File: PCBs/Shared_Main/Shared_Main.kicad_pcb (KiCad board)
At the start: 4 copper layers, 185.4 x 55.9 mm, 53 parts, among them J1 Power, J10 Digital inputs, J11 Digital inputs, J12 Digital inputs, J13 Digital inputs, J14 Digital inputs, J15 Digital inputs, J16 Other unit, J2 Rotary switches pin 1, J4 Aux, J5 Analog inputs, J7 Keypad, Q1 BC547, Q2 BC547, Q3 BC547, Q4 BC547, Q5 BC547, Q6 BC547, Q7 BC547, Q8 BC547, U1 ESP32-S3-ZERO, U2 74HC4051, U4 74HC165, U5 74HC165, U6 74HC165, U7 74HC165, U8 74HC165, U9 74HC165

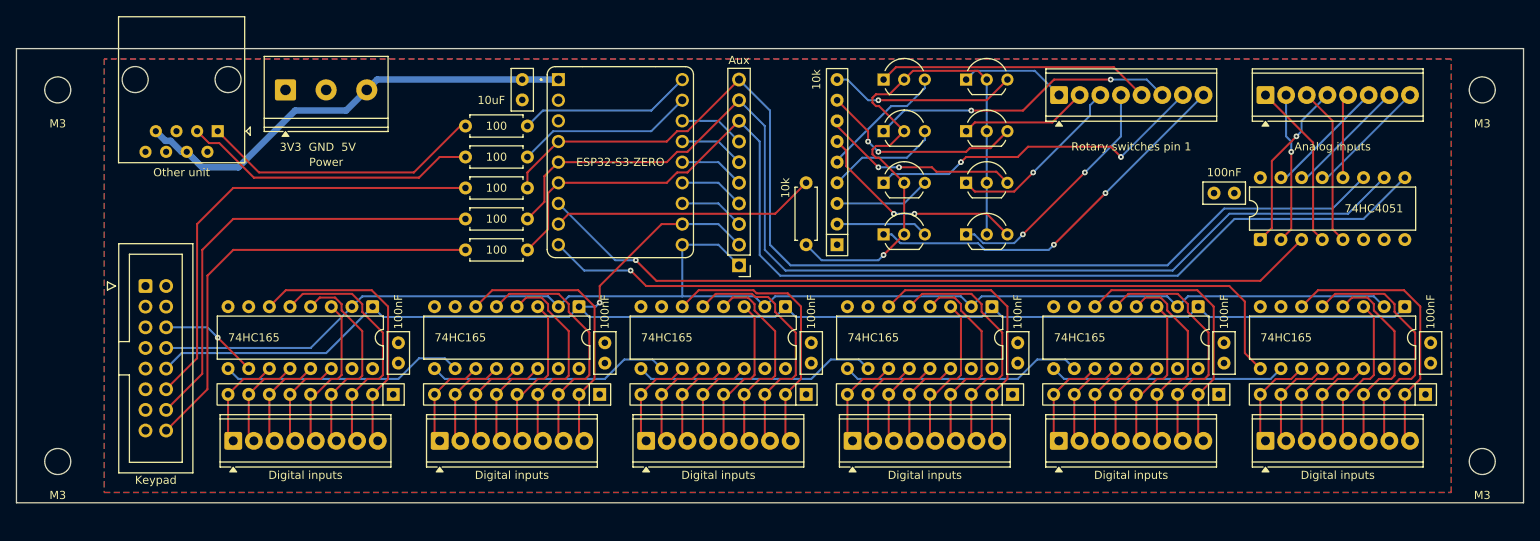
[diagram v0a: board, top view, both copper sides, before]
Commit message: change to vertical spring terminals
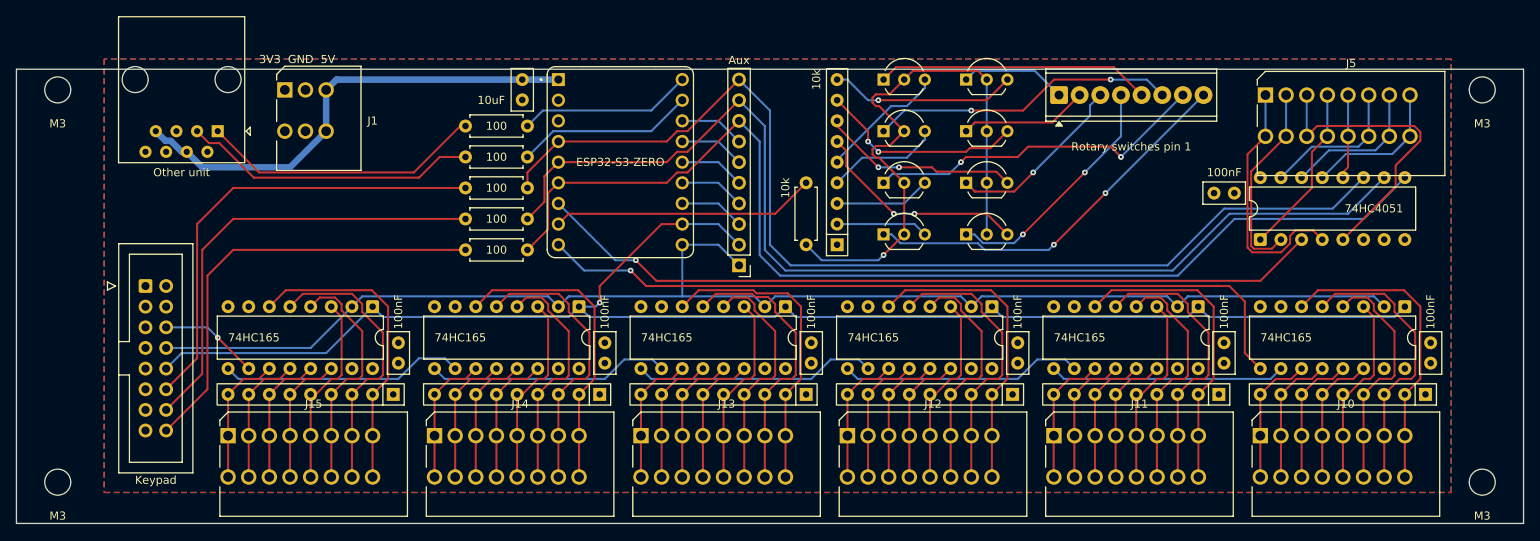
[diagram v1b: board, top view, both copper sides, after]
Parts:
- J1: footprint TerminalBlock_Phoenix:TerminalBlock_Phoenix_PT-1,5-3-5.0-H_1x03_P5.00mm_Horizontal -> Custom_Footprints:SpringTerminal_1x03_P2.54mm_Vertical
- J10, J11, J12, J13, J14, J15, J5: footprint TerminalBlock_Phoenix:TerminalBlock_Phoenix_MPT-0,5-8-2.54_1x08_P2.54mm_Horizontal -> Custom_Footprints:SpringTerminal_1x08_P2.54mm_Vertical
- moved H2 2.54 mm to (234.3, 116.8)
- moved H3 2.54 mm to (59.1, 116.8)
- moved J10 0.90 mm to (207.0, 111.1)
- moved J14 0.90 mm to (105.4, 111.1)
- moved J12 0.90 mm to (156.2, 111.1)
- moved J13 0.90 mm to (130.8, 111.1)
- moved J15 0.90 mm to (80.0, 111.1)
- moved J11 0.88 mm to (181.6, 111.1)
- moved J1 0.08 mm to (87.0, 68.6)
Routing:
- net Net-(J5-Pin_3): track 19.6 -> 37.1 mm
- net Net-(J5-Pin_1): track 20.7 -> 31.2 mm
- net Net-(J5-Pin_2): track 18.6 -> 24.6 mm, vias 1 -> 0
- net Net-(J11-Pin_5): track 18.2 -> 23.3 mm
- net Net-(J11-Pin_1): track 11.5 -> 16.6 mm
- net Net-(J11-Pin_8): track 33.0 -> 38.0 mm
- net Net-(J11-Pin_6): track 24.3 -> 29.4 mm
- net Net-(J11-Pin_4): track 11.5 -> 16.6 mm
- net Net-(J11-Pin_3): track 11.5 -> 16.6 mm
- net Net-(J11-Pin_2): track 11.5 -> 16.6 mm
- net Net-(J11-Pin_7): track 29.7 -> 34.8 mm
- net Net-(J14-Pin_7): track 29.7 -> 34.8 mm
- net Net-(J13-Pin_6): track 24.3 -> 29.4 mm
- net Net-(J13-Pin_7): track 29.7 -> 34.8 mm
- net Net-(J12-Pin_7): track 29.7 -> 34.8 mm
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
